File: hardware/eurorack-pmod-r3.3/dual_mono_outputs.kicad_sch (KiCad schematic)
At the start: 14 parts, among them J8 AUDIO JACK PJ-324M0, J9 AUDIO JACK PJ-324M0, U2 TL074 OP AMP

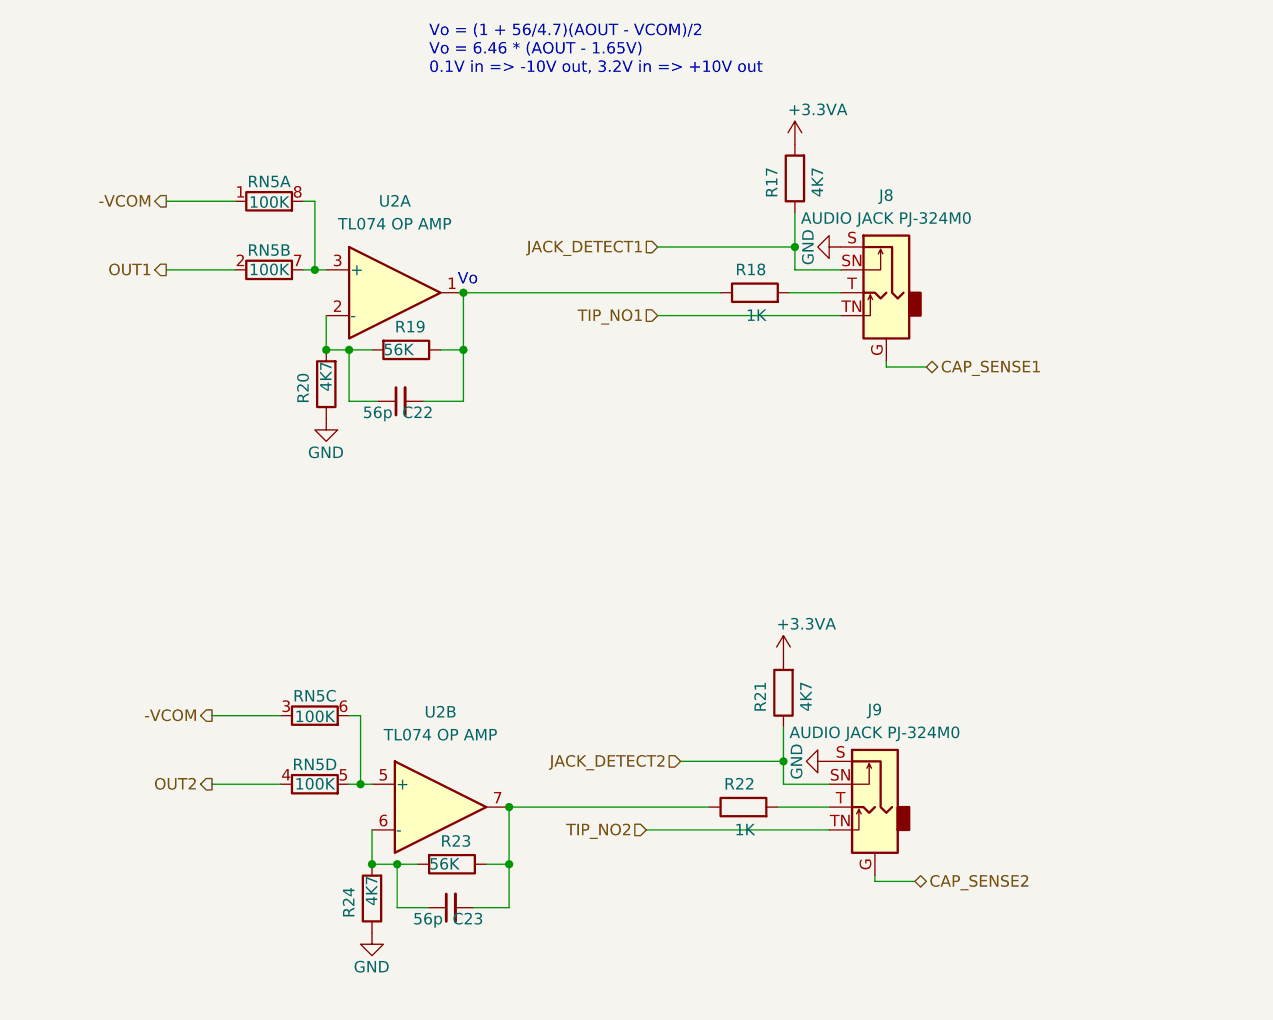
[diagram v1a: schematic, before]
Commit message: - Add ceradiodes to audio ins/outs - Add low-capacitance TVS to touch channels (TODO footprint)
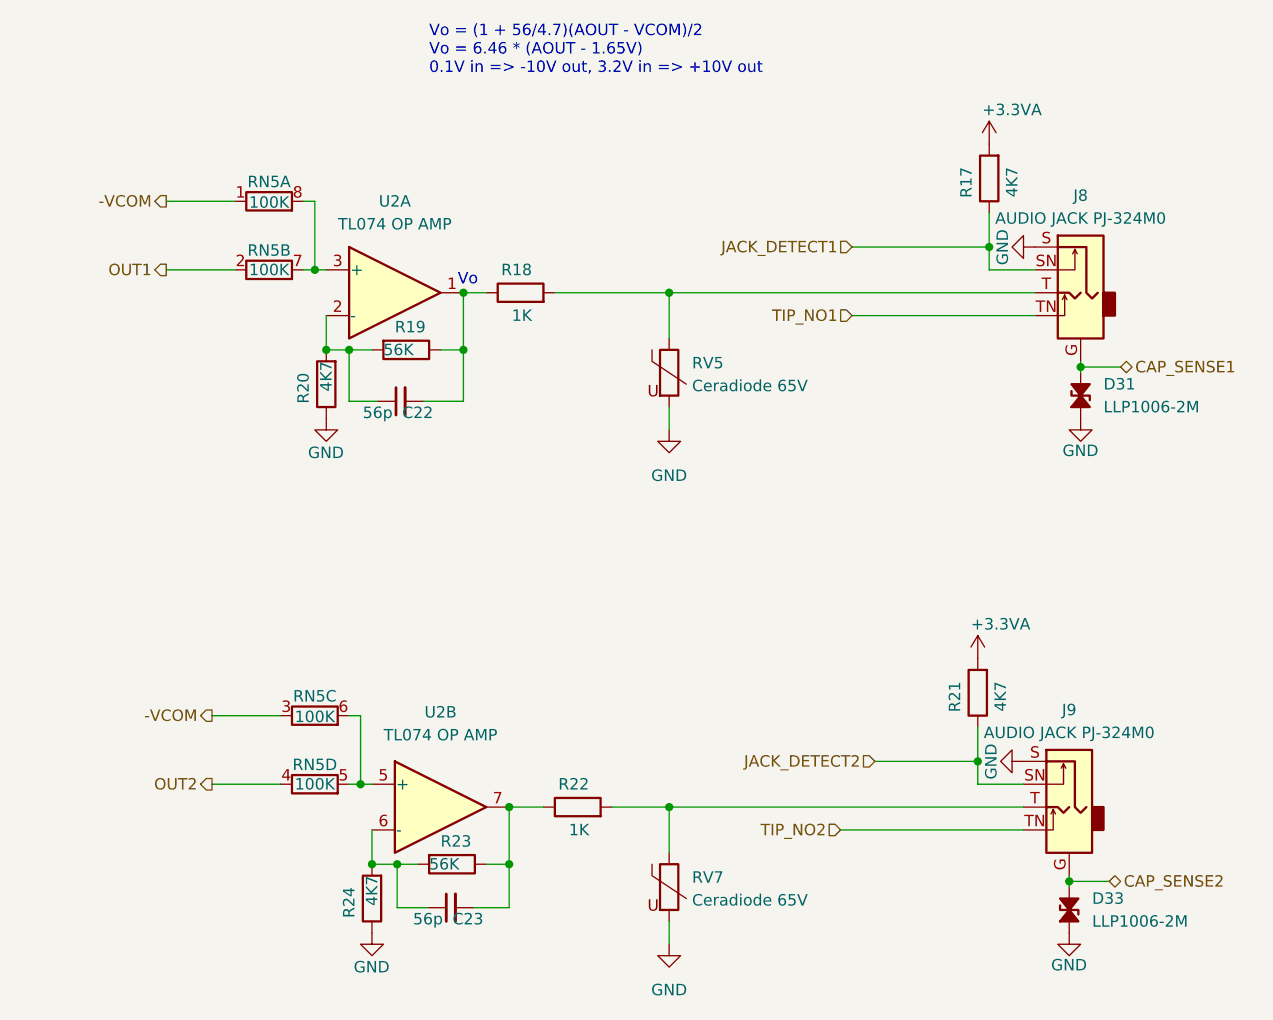
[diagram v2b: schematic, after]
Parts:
- added D31, D33: LLP1006-2M, symbol Device:D_TVS_Small_Filled
- added RV5, RV7: Ceradiode 65V, Capacitor_SMD:C_0603_1608Metric, symbol Device:Varistor
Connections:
- net CAP_SENSE1: now also D31.2 (A2)
- net CAP_SENSE2: now also D33.2 (A2)
- net GND: now also D31.1 (A1), D33.1 (A1), RV5.2, RV7.2
- net at J8.T, R18.2: now also RV5.1
- net at J9.T, R22.2: now also RV7.1
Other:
- moved on the sheet: J8, J9, R17, R18, R21, R22

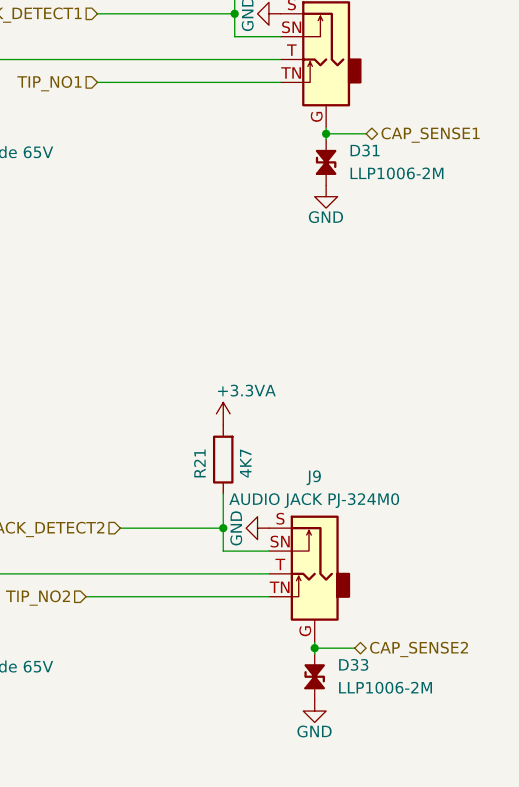
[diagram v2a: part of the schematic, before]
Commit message: - ceradiodes/tvs: place and route
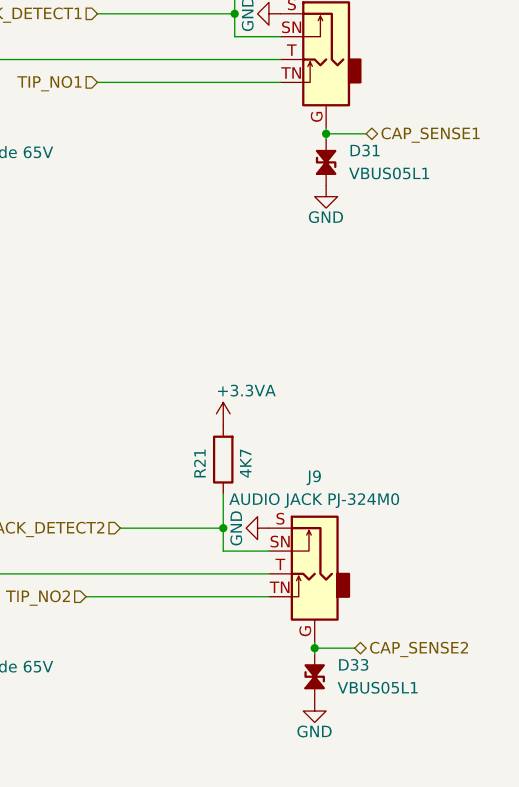
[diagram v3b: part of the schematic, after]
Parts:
- D31, D33: value LLP1006-2M -> VBUS05L1; footprint (none) -> LLP1006-2M:VISHAY-LLP1006-2M
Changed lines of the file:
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@@
 			)
 		)
-		(property "Value" "LLP1006-2M"
+		(property "Value" "VBUS05L1"
 			(at 127 115.5699 90)
 			(effects
@@
 			)
 		)
-		(property "Footprint" ""
+		(property "Footprint" "LLP1006-2M:VISHAY-LLP1006-2M"
 			(at 124.46 114.3 0)
 			(effects
@@
 			)
 		)
-		(property "Value" "LLP1006-2M"
+		(property "Value" "VBUS05L1"
 			(at 128.27 58.4199 90)
 			(effects
@@
 			)
 		)
-		(property "Footprint" ""
+		(property "Footprint" "LLP1006-2M:VISHAY-LLP1006-2M"
 			(at 125.73 57.15 0)
 			(effects

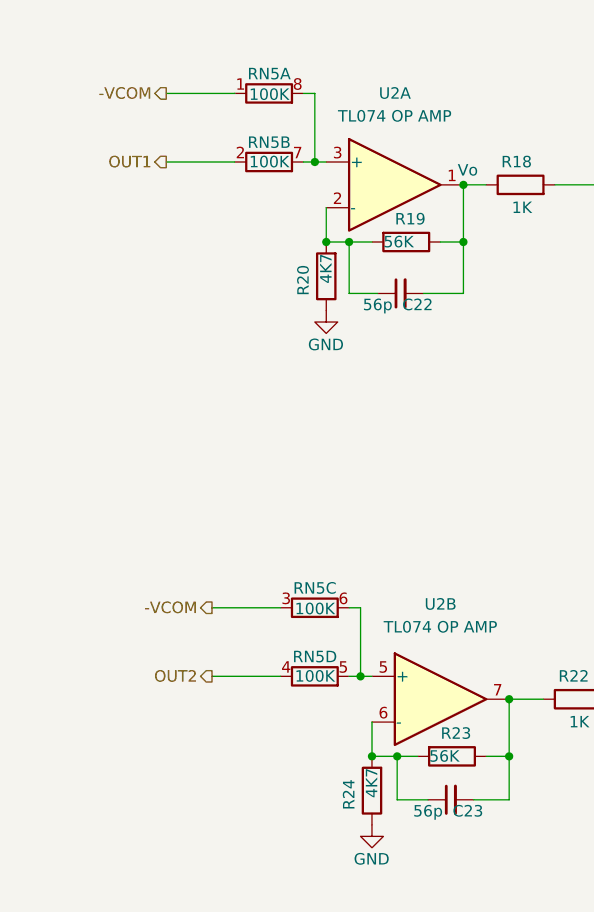
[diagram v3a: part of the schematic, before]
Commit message: - touch: fix XRES on CS6 (!!) - mute: start on JFET output mute
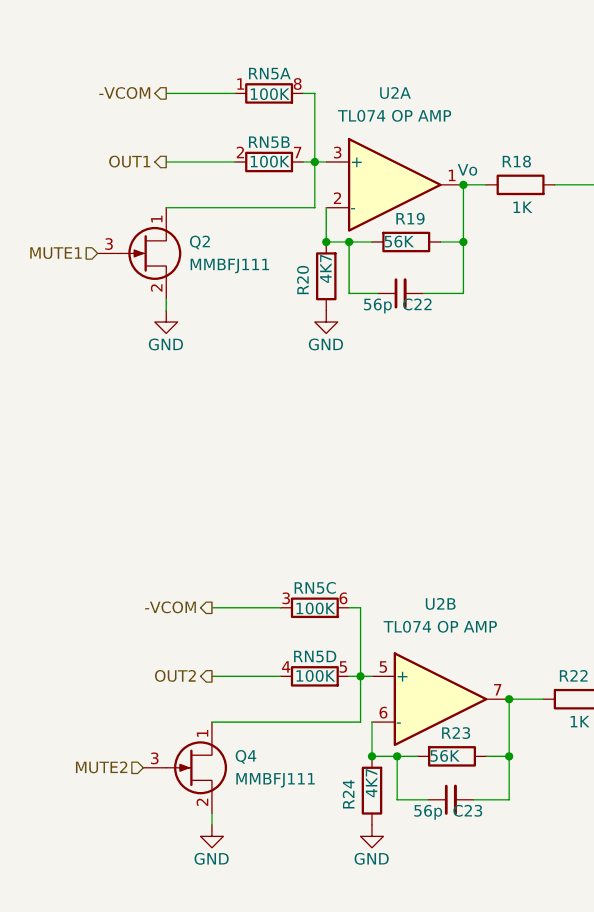
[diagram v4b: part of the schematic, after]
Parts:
- added Q2, Q4: MMBFJ111, Package_TO_SOT_SMD:SOT-23, symbol Transistor_FET:MMBFJ111
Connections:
- net GND: now also Q2.2 (S), Q4.2 (S)
- net at RN5.5 (R4.2), RN5.6 (R3.2), U2.5 (+): now also Q4.1 (D)
- net at RN5.7 (R2.2), RN5.8 (R1.2), U2.3 (+): now also Q2.1 (D)
- new net MUTE1: Q2.3 (G)
- new net MUTE2: Q4.3 (G)

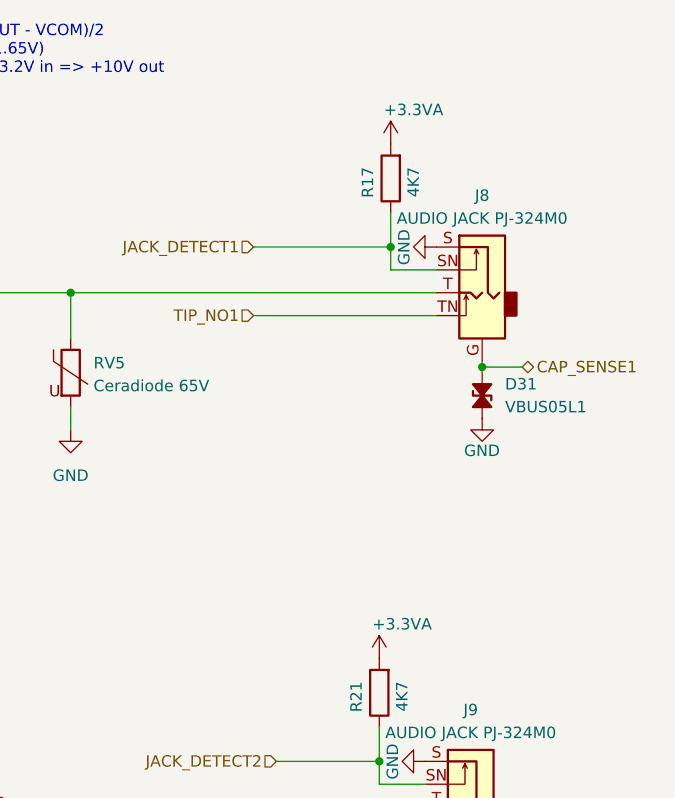
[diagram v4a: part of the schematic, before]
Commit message: vref: replace +3.0V with local 12V->3.3V LDO
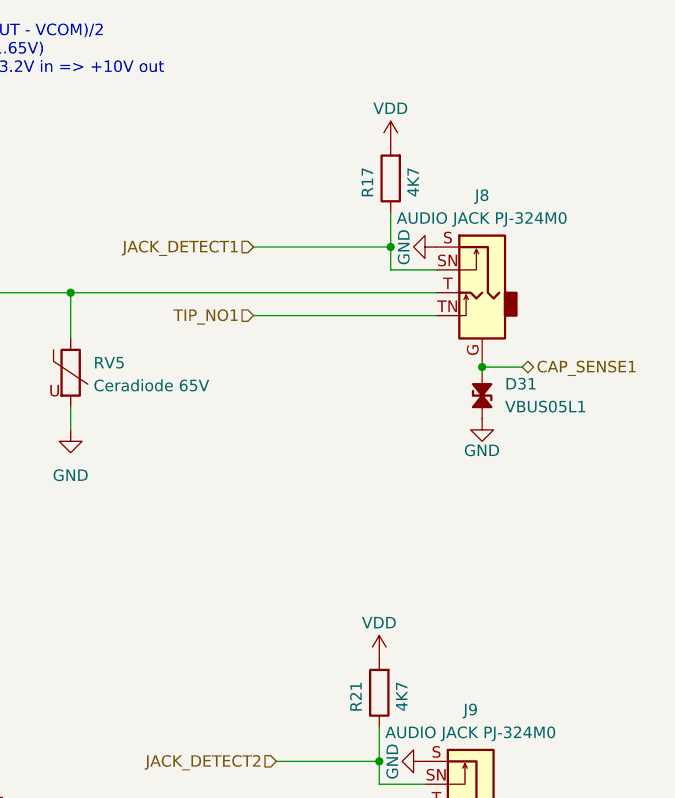
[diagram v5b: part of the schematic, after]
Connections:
- net +3.3VA renamed VDD
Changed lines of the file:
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@@
+	)
+	(symbol
+		(lib_id "power:VDD")
+		(at 114.3 86.36 0)
+		(unit 1)
+		(exclude_from_sim no)
+		(in_bom yes)
+		(on_board yes)
+		(dnp no)
+		(property "Reference" "#PWR083"
+			(at 114.3 90.17 0)
+			(effects
+				(font
+					(size 1.27 1.27)
+				)
+				(hide yes)
+			)
+		)
+		(property "Value" "VDD"
+			(at 114.3 82.423 0)
+			(effects
+				(font
+					(size 1.27 1.27)
+				)
+			)
+		)
+		(property "Footprint" ""
+			(at 114.3 86.36 0)
+			(effects
+				(font
+					(size 1.27 1.27)
+				)
+				(hide yes)
+			)
+		)
+		(property "Datasheet" ""
+			(at 114.3 86.36 0)
+			(effects
+				(font
+					(size 1.27 1.27)
+				)
+				(hide yes)
+			)
+		)
+		(property "Description" ""
+			(at 114.3 86.36 0)
+			(effects
+				(font
+					(size 1.27 1.27)
+				)
+			)
+		)
+		(pin "1"
+		)
+		(instances
+			(project "eurorack-pmod-pcb"
+				(path "/d1469efb-590b-4a61-a37b-5bbc286936ba/62386825-0ccb-4e80-b3cc-940f31e07af6"
+					(reference "#PWR091")
+					(unit 1)
+				)
+				(path "/d1469efb-590b-4a61-a37b-5bbc286936ba/ee8a9905-d244-4108-aba7-f2ec5b742432"
+					(reference "#PWR083")
+					(unit 1)
+				)
+			)
+		)
 	)
 	(symbol
@@
 	)
 	(symbol
-		(lib_id "power:+3.3VA")
-		(at 114.3 86.36 0)
-		(unit 1)
-		(exclude_from_sim no)
-		(in_bom yes)
-		(on_board yes)
-		(dnp no)
-		(property "Reference" "#PWR083"
-			(at 114.3 90.17 0)
-			(effects
-				(font
-					(size 1.27 1.27)
-				)
-				(hide yes)
-			)
-		)
-		(property "Value" "+3.3VA"
-			(at 116.84 82.55 0)
-			(effects
-				(font
-					(size 1.27 1.27)
-				)
-			)
-		)
-		(property "Footprint" ""
-			(at 114.3 86.36 0)
-			(effects
-				(font
-					(size 1.27 1.27)
-				)
-				(hide yes)
-			)
-		)
-		(property "Datasheet" ""
-			(at 114.3 86.36 0)
-			(effects
-				(font
-					(size 1.27 1.27)
-				)
-				(hide yes)
-			)
-		)
-		(property "Description" ""
-			(at 114.3 86.36 0)
-			(effects
-				(font
-					(size 1.27 1.27)
-				)
-			)
-		)
-		(pin "1"
-		)
-		(instances
-			(project "eurorack-pmod-pcb"
-				(path "/d1469efb-590b-4a61-a37b-5bbc286936ba/62386825-0ccb-4e80-b3cc-940f31e07af6"
-					(reference "#PWR091")
-					(unit 1)
-				)
-				(path "/d1469efb-590b-4a61-a37b-5bbc286936ba/ee8a9905-d244-4108-aba7-f2ec5b742432"
-					(reference "#PWR083")
-					(unit 1)
-				)
-			)
-		)
-	)
-	(symbol
 		(lib_id "power:GND")
 		(at 46.99 116.84 0)
@@
 				(path "/d1469efb-590b-4a61-a37b-5bbc286936ba/ee8a9905-d244-4108-aba7-f2ec5b742432"
 					(reference "#PWR086")
+					(unit 1)
+				)
+			)
+		)
+	)
+	(symbol
+		(lib_id "power:VDD")
+		(at 115.57 29.21 0)
+		(unit 1)
+		(exclude_from_sim no)
+		(in_bom yes)
+		(on_board yes)
+		(dnp no)
+		(property "Reference" "#PWR079"
+			(at 115.57 33.02 0)
+			(effects
+				(font
+					(size 1.27 1.27)
+				)
+				(hide yes)
+			)
+		)
+		(property "Value" "VDD"
+			(at 115.57 25.273 0)
+			(effects
+				(font
+					(size 1.27 1.27)
+				)
+			)
+		)
+		(property "Footprint" ""
+			(at 115.57 29.21 0)
+			(effects
+				(font
+					(size 1.27 1.27)
+				)
+				(hide yes)
+			)
+		)
+		(property "Datasheet" ""
+			(at 115.57 29.21 0)
+			(effects
+				(font
+					(size 1.27 1.27)
+				)
+				(hide yes)
+			)
+		)
+		(property "Description" ""
+			(at 115.57 29.21 0)
+			(effects
+				(font
+					(size 1.27 1.27)
+				)
+			)
+		)
+		(pin "1"
+		)
+		(instances
+			(project "eurorack-pmod-pcb"
+				(path "/d1469efb-590b-4a61-a37b-5bbc286936ba/62386825-0ccb-4e80-b3cc-940f31e07af6"
+					(reference "#PWR087")
+					(unit 1)
+				)
+				(path "/d1469efb-590b-4a61-a37b-5bbc286936ba/ee8a9905-d244-4108-aba7-f2ec5b742432"
+					(reference "#PWR079")
 					(unit 1)
 				)
@@
 					(unit 1)
 				)
-			)
-		)
-	)
-	(symbol
-		(lib_id "power:+3.3VA")
-		(at 115.57 29.21 0)
-		(unit 1)
-		(exclude_from_sim no)
-		(in_bom yes)
-		(on_board yes)
-		(dnp no)
-		(property "Reference" "#PWR079"
-			(at 115.57 33.02 0)
-			(effects
-				(font
-					(size 1.27 1.27)
-				)
-				(hide yes)
-			)
-		)
-		(property "Value" "+3.3VA"
-			(at 118.11 25.4 0)
-			(effects
-				(font
-					(size 1.27 1.27)
-				)
-			)
-		)
-		(property "Footprint" ""
-			(at 115.57 29.21 0)
-			(effects
-				(font
-					(size 1.27 1.27)
-				)
-				(hide yes)
-			)
-		)
-		(property "Datasheet" ""
-			(at 115.57 29.21 0)
-			(effects
-				(font
-					(size 1.27 1.27)
-				)
-				(hide yes)
-			)
-		)
-		(property "Description" ""
-			(at 115.57 29.21 0)
-			(effects
-				(font
-					(size 1.27 1.27)
-				)
-			)
-		)
-		(pin "1"
-		)
-		(instances
-			(project "eurorack-pmod-pcb"
-				(path "/d1469efb-590b-4a61-a37b-5bbc286936ba/62386825-0ccb-4e80-b3cc-940f31e07af6"
-					(reference "#PWR087")
-					(unit 1)
-				)
-				(path "/d1469efb-590b-4a61-a37b-5bbc286936ba/ee8a9905-d244-4108-aba7-f2ec5b742432"
-					(reference "#PWR079")
-					(unit 1)
-				)
